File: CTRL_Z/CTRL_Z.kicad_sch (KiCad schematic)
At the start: 6 parts, among them J1 BM04B-NSHSS-TBT_LF__SN_

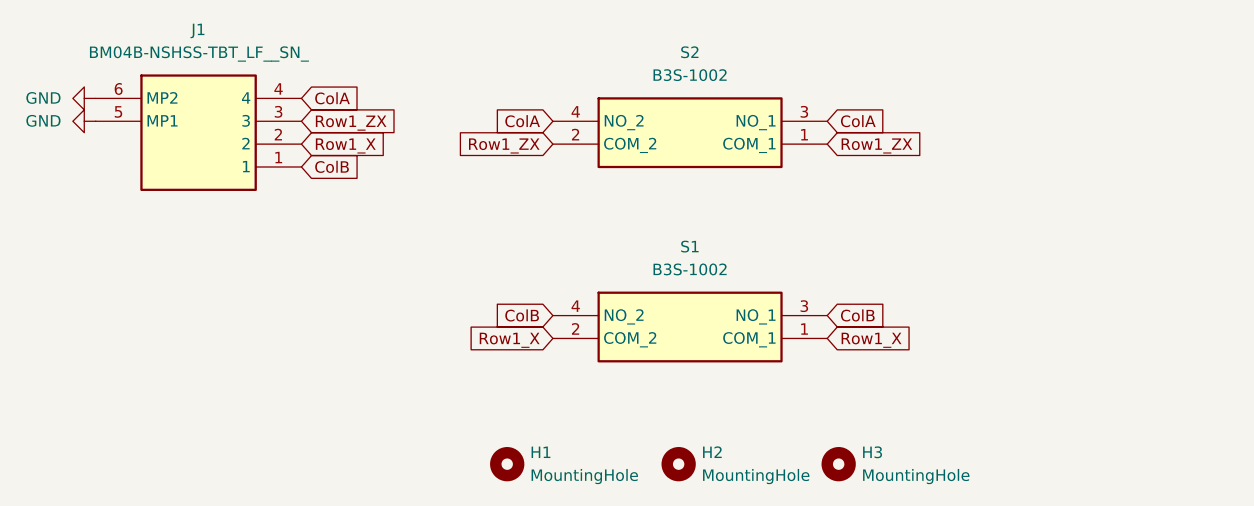
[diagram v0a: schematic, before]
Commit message: CTRL Z, R, PWR Cleanup! Changes Made:
CTRL PWR -> Added Ground Plane and Ground Vias. Moved it out of parent folder CTRL_R upto Root.
CTRL Z ->  Removed Unnecessary ZX pin. Added Ground Plane and Ground Vias.
CTRL R -> Cleaned up pin count, from 14 down to 10. Added Ground Plane and Ground Vias. Made some modifications to the board shape.
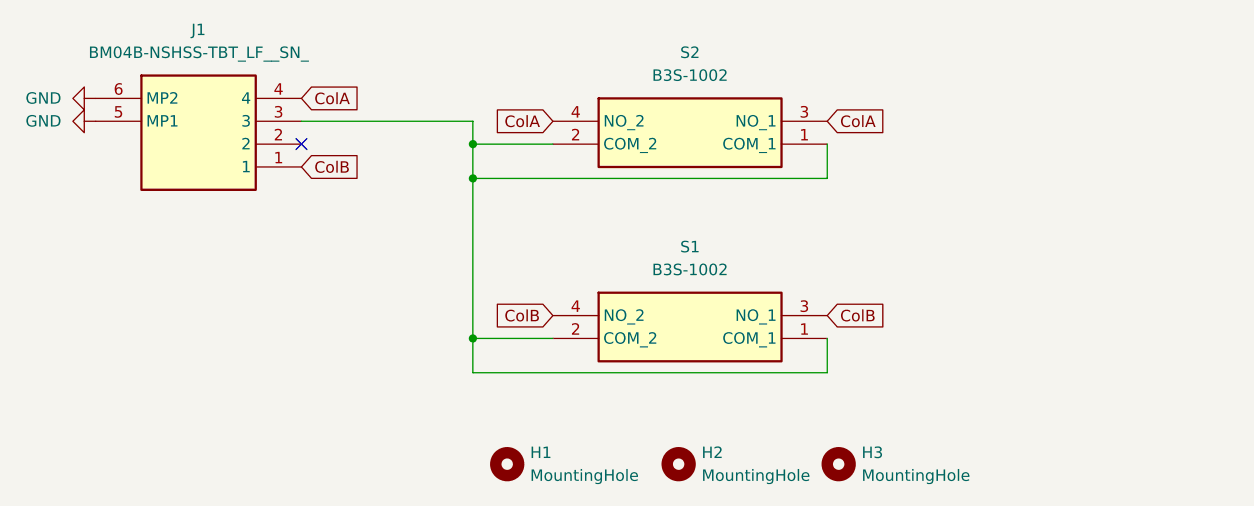
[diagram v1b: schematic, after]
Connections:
- net Row1_ZX is gone; now on an unnamed net: J1.3, S2.1 (COM_1), S2.2 (COM_2)
- net Row1_X: no longer names the net of S1.1 (COM_1), S1.2 (COM_2)
- net Row1_X: no longer J1.2
- no-connect marks 0 -> 1
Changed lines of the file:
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@@
 	(generator_version "10.0")
 	(paper "A4")
+	(junction
+		(at 80.01 114.3)
+		(diameter 0)
+		(color 0 0 0 0)
+	)
+	(junction
+		(at 80.01 92.71)
+		(diameter 0)
+		(color 0 0 0 0)
+	)
+	(junction
+		(at 80.01 96.52)
+		(diameter 0)
+		(color 0 0 0 0)
+	)
+	(no_connect
+		(at 60.96 92.71)
+	)
+	(wire
+		(pts
+			(xy 80.01 114.3) (xy 80.01 118.11)
+		)
+		(stroke
+			(width 0)
+			(type default)
+		)
+	)
+	(wire
+		(pts
+			(xy 80.01 92.71) (xy 88.9 92.71)
+		)
+		(stroke
+			(width 0)
+			(type default)
+		)
+	)
+	(wire
+		(pts
+			(xy 119.38 92.71) (xy 119.38 96.52)
+		)
+		(stroke
+			(width 0)
+			(type default)
+		)
+	)
+	(wire
+		(pts
+			(xy 60.96 90.17) (xy 80.01 90.17)
+		)
+		(stroke
+			(width 0)
+			(type default)
+		)
+	)
+	(wire
+		(pts
+			(xy 80.01 96.52) (xy 80.01 114.3)
+		)
+		(stroke
+			(width 0)
+			(type default)
+		)
+	)
+	(wire
+		(pts
+			(xy 119.38 96.52) (xy 80.01 96.52)
+		)
+		(stroke
+			(width 0)
+			(type default)
+		)
+	)
+	(wire
+		(pts
+			(xy 119.38 118.11) (xy 119.38 114.3)
+		)
+		(stroke
+			(width 0)
+			(type default)
+		)
+	)
+	(wire
+		(pts
+			(xy 80.01 118.11) (xy 119.38 118.11)
+		)
+		(stroke
+			(width 0)
+			(type default)
+		)
+	)
+	(wire
+		(pts
+			(xy 80.01 90.17) (xy 80.01 92.71)
+		)
+		(stroke
+			(width 0)
+			(type default)
+		)
+	)
+	(wire
+		(pts
+			(xy 80.01 114.3) (xy 88.9 114.3)
+		)
+		(stroke
+			(width 0)
+			(type default)
+		)
+	)
+	(wire
+		(pts
+			(xy 80.01 92.71) (xy 80.01 96.52)
+		)
+		(stroke
+			(width 0)
+			(type default)
+		)
+	)
 	(global_label "ColA"
 		(shape input)
@@
 		)
 	)
-	(global_label "Row1_X"
-		(shape input)
-		(at 88.9 114.3 180)
+	(global_label "ColB"
+		(shape input)
+		(at 60.96 95.25 0)
+		(fields_autoplaced yes)
+		(effects
+			(font
+				(size 1.27 1.27)
+			)
+			(justify left)
+		)
+		(property "Intersheetrefs" "${INTERSHEET_REFS}"
+			(at 68.2994 95.25 0)
+			(hide yes)
+			(show_name no)
+			(do_not_autoplace no)
+			(effects
+				(font
+					(size 1.27 1.27)
+				)
+				(justify left)
+			)
+		)
+	)
+	(global_label "ColB"
+		(shape input)
+		(at 88.9 111.76 180)
 		(fields_autoplaced yes)
 		(effects
@@
 		)
 		(property "Intersheetrefs" "${INTERSHEET_REFS}"
-			(at 78.7787 114.3 0)
+			(at 81.5606 111.76 0)
 			(hide yes)
 			(show_name no)
@@
 		)
 	)
-	(global_label "Row1_X"
-		(shape input)
-		(at 119.38 114.3 0)
-		(fields_autoplaced yes)
-		(effects
-			(font
-				(size 1.27 1.27)
-			)
-			(justify left)
-		)
-		(property "Intersheetrefs" "${INTERSHEET_REFS}"
-			(at 129.5013 114.3 0)
-			(hide yes)
-			(show_name no)
-			(do_not_autoplace no)
-			(effects
-				(font
-					(size 1.27 1.27)
-				)
-				(justify left)
-			)
-		)
-	)
-	(global_label "ColB"
-		(shape input)
-		(at 60.96 95.25 0)
-		(fields_autoplaced yes)
-		(effects
-			(font
-				(size 1.27 1.27)
-			)
-			(justify left)
-		)
-		(property "Intersheetrefs" "${INTERSHEET_REFS}"
-			(at 68.2994 95.25 0)
-			(hide yes)
-			(show_name no)
-			(do_not_autoplace no)
-			(effects
-				(font
-					(size 1.27 1.27)
-				)
-				(justify left)
-			)
-		)
-	)
-	(global_label "Row1_ZX"
-		(shape input)
-		(at 88.9 92.71 180)
+	(global_label "ColA"
+		(shape input)
+		(at 88.9 90.17 180)
 		(fields_autoplaced yes)
 		(effects
@@
 		)
 		(property "Intersheetrefs" "${INTERSHEET_REFS}"
-			(at 77.5692 92.71 0)
+			(at 81.742 90.17 0)
 			(hide yes)
 			(show_name no)
@@
 			)
 		)
-	)
-	(global_label "Row1_ZX"
-		(shape input)
-		(at 119.38 92.71 0)
-		(fields_autoplaced yes)
-		(effects
-			(font
-				(size 1.27 1.27)
-			)
-			(justify left)
-		)
-		(property "Intersheetrefs" "${INTERSHEET_REFS}"
-			(at 130.7108 92.71 0)
-			(hide yes)
-			(show_name no)
-			(do_not_autoplace no)
-			(effects
-				(font
-					(size 1.27 1.27)
-				)
-				(justify left)
-			)
-		)
-	)
-	(global_label "ColB"
-		(shape input)
-		(at 88.9 111.76 180)
-		(fields_autoplaced yes)
-		(effects
-			(font
-				(size 1.27 1.27)
-			)
-			(justify right)
-		)
-		(property "Intersheetrefs" "${INTERSHEET_REFS}"
-			(at 81.5606 111.76 0)
-			(hide yes)
-			(show_name no)
-			(do_not_autoplace no)
-			(effects
-				(font
-					(size 1.27 1.27)
-				)
-				(justify right)
-			)
-		)
-	)
-	(global_label "ColA"
-		(shape input)
-		(at 88.9 90.17 180)
-		(fields_autoplaced yes)
-		(effects
-			(font
-				(size 1.27 1.27)
-			)
-			(justify right)
-		)
-		(property "Intersheetrefs" "${INTERSHEET_REFS}"
-			(at 81.742 90.17 0)
-			(hide yes)
-			(show_name no)
-			(do_not_autoplace no)
-			(effects
-				(font
-					(size 1.27 1.27)
-				)
-				(justify right)
-			)
-		)
-	)
-	(global_label "Row1_ZX"
-		(shape input)
-		(at 60.96 90.17 0)
-		(fields_autoplaced yes)
-		(effects
-			(font
-				(size 1.27 1.27)
-			)
-			(justify left)
-		)
-		(property "Intersheetrefs" "${INTERSHEET_REFS}"
-			(at 72.2908 90.17 0)
-			(hide yes)
-			(show_name no)
-			(do_not_autoplace no)
-			(effects
-				(font
-					(size 1.27 1.27)
-				)
-				(justify left)
-			)
-		)
-	)
-	(global_label "Row1_X"
-		(shape input)
-		(at 60.96 92.71 0)
-		(fields_autoplaced yes)
-		(effects
-			(font
-				(size 1.27 1.27)
-			)
-			(justify left)
-		)
-		(property "Intersheetrefs" "${INTERSHEET_REFS}"
-			(at 71.0813 92.71 0)
-			(hide yes)
-			(show_name no)
-			(do_not_autoplace no)
-			(effects
-				(font
-					(size 1.27 1.27)
-				)
-				(justify left)
-			)
-		)

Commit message: Updated CTRL_Z to use 3 pin FPC and ESD Protection.
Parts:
- removed J1: BM04B-NSHSS-TBT_LF__SN_, BM04B-NSHSS-TBT:BM04BNSHSSTBTLFSN, symbol BM04B-NSHSS-TBT_LF__SN_:BM04B-NSHSS-TBT_LF__SN_
- added D22, D23, D24, D25: ESD5V0B03, A_HDJ_Library:D_0402_1005Metric, symbol Diode:ESD9B5.0ST5G
- added J1: AYF530365TA, AYF530365TA:AYF530365T, symbol AYF530365TA:AYF530365TA
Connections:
- net ColA: now also D24.2 (A2), J1.3
- net ColB: now also D25.2 (A2), J1.1
- net GND: now also D22.1 (A1), D23.1 (A1), D24.1 (A1), D25.1 (A1), J1.4 (MP1), J1.5 (MP2)
- net at S1.1 (COM_1), S1.2 (COM_2), S2.1 (COM_1)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: now also D22.2 (A2), D23.2 (A2), J1.2
- no-connect marks 1 -> 0
